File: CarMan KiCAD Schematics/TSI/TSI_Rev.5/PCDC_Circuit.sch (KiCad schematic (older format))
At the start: 56 parts, among them IC4 TS431ILT, K1 APAN3105, Q1 ZVP1320F, Q5 SI1302DL-T1-E3, U10 74LS00PowerPins, U12 REF3033, U19 74HC00, U20 MC7805BDTRKG, U21 MCP6004, U29 SN74LVC1G08DCKR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

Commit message: Added footprints for MCP6004
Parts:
- U21, U35, U40: footprint (none) -> TSI_Rev_2021_Footprint_Lib:SOIC127P600X175-14N
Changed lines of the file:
@@
 F 0 "U21" H 3950 3600 50  0000 C CNN
 F 1 "MCP6004" H 4150 3450 50  0000 C CNN
-F 2 "" H 3950 3700 50  0001 C CNN
+F 2 "TSI_Rev_2021_Footprint_Lib:SOIC127P600X175-14N" H 3950 3700 50  0001 C CNN
 F 3 "http://ww1.microchip.com/downloads/en/DeviceDoc/21733j.pdf" H 4050 3800 50  0001 C CNN
 	4    4000 3600
@@
 F 0 "U21" H 3950 2750 50  0000 C CNN
 F 1 "MCP6004" H 4150 2600 50  0000 C CNN
-F 2 "" H 3950 2850 50  0001 C CNN
+F 2 "TSI_Rev_2021_Footprint_Lib:SOIC127P600X175-14N" H 3950 2850 50  0001 C CNN
 F 3 "http://ww1.microchip.com/downloads/en/DeviceDoc/21733j.pdf" H 4050 2950 50  0001 C CNN
 	3    4000 2750
@@
 F 0 "U40" H 5308 2896 50  0001 L CNN
 F 1 "MCP6004" H 5308 2850 50  0001 L CNN
-F 2 "" H 5300 2950 50  0001 C CNN
+F 2 "TSI_Rev_2021_Footprint_Lib:SOIC127P600X175-14N" H 5300 2950 50  0001 C CNN
 F 3 "http://ww1.microchip.com/downloads/en/DeviceDoc/21733j.pdf" H 5400 3050 50  0001 C CNN
 	5    5350 2850
@@
 F 0 "U40" H 5400 2850 50  0000 C CNN
 F 1 "MCP6004" H 5500 3000 50  0000 C CNN
-F 2 "" H 5300 2950 50  0001 C CNN
+F 2 "TSI_Rev_2021_Footprint_Lib:SOIC127P600X175-14N" H 5300 2950 50  0001 C CNN
 F 3 "http://ww1.microchip.com/downloads/en/DeviceDoc/21733j.pdf" H 5400 3050 50  0001 C CNN
 	1    5350 2850
@@
 F 0 "U40" H 5350 3500 50  0000 C CNN
 F 1 "MCP6004" H 5450 3700 50  0000 C CNN
-F 2 "" H 5300 3600 50  0001 C CNN
+F 2 "TSI_Rev_2021_Footprint_Lib:SOIC127P600X175-14N" H 5300 3600 50  0001 C CNN
 F 3 "http://ww1.microchip.com/downloads/en/DeviceDoc/21733j.pdf" H 5400 3700 50  0001 C CNN
 	2    5350 3500
@@
 F 0 "U40" H 10550 4150 50  0000 C CNN
 F 1 "MCP6004" H 10550 4426 50  0000 C CNN
-F 2 "" H 10500 4250 50  0001 C CNN
+F 2 "TSI_Rev_2021_Footprint_Lib:SOIC127P600X175-14N" H 10500 4250 50  0001 C CNN
 F 3 "http://ww1.microchip.com/downloads/en/DeviceDoc/21733j.pdf" H 10600 4350 50  0001 C CNN
 	4    10550 4150
@@
 F 0 "U35" H 3650 8300 50  0000 C CNN
 F 1 "MCP6004" H 3850 8450 50  0000 C CNN
-F 2 "" H 3600 8400 50  0001 C CNN
+F 2 "TSI_Rev_2021_Footprint_Lib:SOIC127P600X175-14N" H 3600 8400 50  0001 C CNN
 F 3 "http://ww1.microchip.com/downloads/en/DeviceDoc/21733j.pdf" H 3700 8500 50  0001 C CNN
 	1    3650 8300
@@
 F 0 "U35" H 3608 8300 50  0001 L CNN
 F 1 "MCP6004" H 3608 8255 50  0001 L CNN
-F 2 "" H 3600 8400 50  0001 C CNN
+F 2 "TSI_Rev_2021_Footprint_Lib:SOIC127P600X175-14N" H 3600 8400 50  0001 C CNN
 F 3 "http://ww1.microchip.com/downloads/en/DeviceDoc/21733j.pdf" H 3700 8500 50  0001 C CNN
 	5    3650 8300

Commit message: TSI Footprints - Res, Caps, Inductor all 0805s - Mounting Holes
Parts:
- C1, C12, C2, C54, C55: footprint (none) -> Capacitor_SMD:C_0805_2012Metric_Pad1.15x1.40mm_HandSolder
- L1: footprint (none) -> Inductor_SMD:L_0805_2012Metric_Pad1.15x1.40mm_HandSolder
- PS1: footprint TSI_Rev_2021_Footprint_Lib:DIP762W50P254L730H410Q6 -> (none)
- R101, R108, R109, R111, R112, R2, R33, R4, R46, R47, R54, R56, R67, R69, R70, R73, R75: footprint (none) -> Resistor_SMD:R_0805_2012Metric_Pad1.15x1.40mm_HandSolder
- U29: footprint SOT65P210X110-5N -> TSI_Rev_2021_Footprint_Lib:SOT65P210X110-5N
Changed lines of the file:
@@
 F 0 "R2" H 4570 1996 50  0000 L CNN
 F 1 "95K" V 4500 1900 50  0000 L CNN
-F 2 "" V 4430 1950 50  0001 C CNN
+F 2 "Resistor_SMD:R_0805_2012Metric_Pad1.15x1.40mm_HandSolder" V 4430 1950 50  0001 C CNN
 F 3 "~" H 4500 1950 50  0001 C CNN
 	1    4500 1950
@@
 F 0 "C55" V 6450 2350 50  0000 C CNN
 F 1 "0.1u" V 6450 2050 50  0000 C CNN
-F 2 "" H 6550 2200 50  0001 C CNN
+F 2 "Capacitor_SMD:C_0805_2012Metric_Pad1.15x1.40mm_HandSolder" H 6550 2200 50  0001 C CNN
 F 3 "~" H 6550 2200 50  0001 C CNN
 	1    6550 2200
@@
 F 0 "R4" V 9750 3050 50  0000 C CNN
 F 1 "5K" V 9850 3050 50  0000 C CNN
-F 2 "" V 9780 3050 50  0001 C CNN
+F 2 "Resistor_SMD:R_0805_2012Metric_Pad1.15x1.40mm_HandSolder" V 9780 3050 50  0001 C CNN
 F 3 "~" H 9850 3050 50  0001 C CNN
 	1    9850 3050
@@
 F 0 "R56" V 9400 3850 50  0000 C CNN
 F 1 "56K" V 9500 3850 50  0000 C CNN
-F 2 "" V 9430 3850 50  0001 C CNN
+F 2 "Resistor_SMD:R_0805_2012Metric_Pad1.15x1.40mm_HandSolder" V 9430 3850 50  0001 C CNN
 F 3 "~" H 9500 3850 50  0001 C CNN
 	1    9500 3850
@@
 F 0 "C54" H 9600 4250 50  0000 C CNN
 F 1 "15u" H 9600 4450 50  0000 C CNN
-F 2 "" H 9500 4350 50  0001 C CNN
+F 2 "Capacitor_SMD:C_0805_2012Metric_Pad1.15x1.40mm_HandSolder" H 9500 4350 50  0001 C CNN
 F 3 "~" H 9500 4350 50  0001 C CNN
 	1    9500 4350
@@
 F 0 "R67" V 10400 2250 50  0000 C CNN
 F 1 "2.4K" V 10500 2250 50  0000 C CNN
-F 2 "" V 10430 2250 50  0001 C CNN
+F 2 "Resistor_SMD:R_0805_2012Metric_Pad1.15x1.40mm_HandSolder" V 10430 2250 50  0001 C CNN
 F 3 "~" H 10500 2250 50  0001 C CNN
 	1    10500 2250
@@
 F 0 "R69" V 12500 3250 50  0000 C CNN
 F 1 "500" V 12600 3250 50  0000 C CNN
-F 2 "" V 12530 3250 50  0001 C CNN
+F 2 "Resistor_SMD:R_0805_2012Metric_Pad1.15x1.40mm_HandSolder" V 12530 3250 50  0001 C CNN
 F 3 "~" H 12600 3250 50  0001 C CNN
 	1    12600 3250
@@
 F 0 "R111" V 6350 6250 50  0000 L CNN
 F 1 "10K" V 6250 6300 50  0000 L CNN
-F 2 "" V 6180 6350 50  0001 C CNN
+F 2 "Resistor_SMD:R_0805_2012Metric_Pad1.15x1.40mm_HandSolder" V 6180 6350 50  0001 C CNN
 F 3 "~" H 6250 6350 50  0001 C CNN
 	1    6250 6350
@@
 F 0 "R109" V 7300 6000 50  0000 L CNN
 F 1 "1M" V 7200 6050 50  0000 L CNN
-F 2 "" V 7130 6100 50  0001 C CNN
+F 2 "Resistor_SMD:R_0805_2012Metric_Pad1.15x1.40mm_HandSolder" V 7130 6100 50  0001 C CNN
 F 3 "~" H 7200 6100 50  0001 C CNN
 	1    7200 6100
@@
 F 0 "R108" V 5200 6250 50  0000 L CNN
 F 1 "2.4K" V 5100 6250 50  0000 L CNN
-F 2 "" V 5030 6350 50  0001 C CNN
+F 2 "Resistor_SMD:R_0805_2012Metric_Pad1.15x1.40mm_HandSolder" V 5030 6350 50  0001 C CNN
 F 3 "~" H 5100 6350 50  0001 C CNN
 	1    5100 6350
@@
 F 0 "R70" V 5200 7050 50  0000 L CNN
 F 1 "2.4K" V 5100 7050 50  0000 L CNN
-F 2 "" V 5030 7150 50  0001 C CNN
+F 2 "Resistor_SMD:R_0805_2012Metric_Pad1.15x1.40mm_HandSolder" V 5030 7150 50  0001 C CNN
 F 3 "~" H 5100 7150 50  0001 C CNN
 	1    5100 7150
@@
 F 0 "C1" H 11650 9150 50  0000 L CNN
 F 1 "0.47u" H 11650 8950 50  0000 L CNN
-F 2 "" H 11600 9050 50  0001 C CNN
+F 2 "Capacitor_SMD:C_0805_2012Metric_Pad1.15x1.40mm_HandSolder" H 11600 9050 50  0001 C CNN
 F 3 "~" H 11600 9050 50  0001 C CNN
 	1    11600 9050
@@
 F 0 "R33" V 5200 10300 50  0000 L CNN
 F 1 "5K" V 5100 10350 50  0000 L CNN
-F 2 "" V 5030 10400 50  0001 C CNN
+F 2 "Resistor_SMD:R_0805_2012Metric_Pad1.15x1.40mm_HandSolder" V 5030 10400 50  0001 C CNN
 F 3 "~" H 5100 10400 50  0001 C CNN
 	1    5100 10400
@@
 F 0 "R54" V 6450 10500 50  0000 L CNN
 F 1 "2.4K" V 6350 10500 50  0000 L CNN
-F 2 "" V 6280 10600 50  0001 C CNN
+F 2 "Resistor_SMD:R_0805_2012Metric_Pad1.15x1.40mm_HandSolder" V 6280 10600 50  0001 C CNN
 F 3 "~" H 6350 10600 50  0001 C CNN
 	1    6350 10600
@@
 F 0 "PS1" H 5725 10081 79  0000 C CNN
 F 1 "THN_30-2415WI" H 5725 9946 79  0000 C CNN
-F 2 "TSI_Rev_2021_Footprint_Lib:DIP762W50P254L730H410Q6" H 5500 9700 79  0001 C CNN
+F 2 "" H 5500 9700 79  0001 C CNN
 F 3 "https://www.snapeda.com/parts/THN%2030-2415WI/Traco%20Power/datasheet/" H 5500 9700 79  0001 C CNN
 	1    5750 9650
@@
 F 0 "R73" V 6350 8600 50  0000 L CNN
 F 1 "5K" V 6250 8650 50  0000 L CNN
-F 2 "" V 6180 8700 50  0001 C CNN
+F 2 "Resistor_SMD:R_0805_2012Metric_Pad1.15x1.40mm_HandSolder" V 6180 8700 50  0001 C CNN
 F 3 "~" H 6250 8700 50  0001 C CNN
 	1    6250 8700
@@
 F 0 "R75" V 6350 7450 50  0000 L CNN
 F 1 "5K" V 6250 7500 50  0000 L CNN
-F 2 "" V 6180 7550 50  0001 C CNN
+F 2 "Resistor_SMD:R_0805_2012Metric_Pad1.15x1.40mm_HandSolder" V 6180 7550 50  0001 C CNN
 F 3 "~" H 6250 7550 50  0001 C CNN
 	1    6250 7550
@@
 F 0 "R112" V 3400 7550 50  0000 L CNN
 F 1 "330" V 3300 7600 50  0000 L CNN
-F 2 "" V 3230 7650 50  0001 C CNN
+F 2 "Resistor_SMD:R_0805_2012Metric_Pad1.15x1.40mm_HandSolder" V 3230 7650 50  0001 C CNN
 F 3 "~" H 3300 7650 50  0001 C CNN
 	1    3300 7650
@@
 F 0 "C12" H 14600 8950 50  0000 C CNN
 F 1 "0.33u" H 14600 9150 50  0000 C CNN
-F 2 "" H 14500 9050 50  0001 C CNN
+F 2 "Capacitor_SMD:C_0805_2012Metric_Pad1.15x1.40mm_HandSolder" H 14500 9050 50  0001 C CNN
 F 3 "~" H 14500 9050 50  0001 C CNN
 	1    14500 9050
@@
 F 0 "R46" V 12800 7650 50  0000 L CNN
 F 1 "1K" V 12700 7700 50  0000 L CNN
-F 2 "" V 12630 7750 50  0001 C CNN
+F 2 "Resistor_SMD:R_0805_2012Metric_Pad1.15x1.40mm_HandSolder" V 12630 7750 50  0001 C CNN
 F 3 "~" H 12700 7750 50  0001 C CNN
 	1    12700 7750
@@
 F 0 "R101" V 14450 7850 50  0000 L CNN
 F 1 "10K" V 14350 7900 50  0000 L CNN
-F 2 "" V 14280 7950 50  0001 C CNN
+F 2 "Resistor_SMD:R_0805_2012Metric_Pad1.15x1.40mm_HandSolder" V 14280 7950 50  0001 C CNN
 F 3 "~" H 14350 7950 50  0001 C CNN
 	1    14350 7950
@@
 F 0 "R47" V 5200 8200 50  0000 L CNN
 F 1 "500" V 5100 8200 50  0000 L CNN
-F 2 "" V 5030 8300 50  0001 C CNN
+F 2 "Resistor_SMD:R_0805_2012Metric_Pad1.15x1.40mm_HandSolder" V 5030 8300 50  0001 C CNN
 F 3 "~" H 5100 8300 50  0001 C CNN
 	1    5100 8300
@@
 F 0 "U29" H 6350 4100 50  0000 C CNN
 F 1 "SN74LVC1G08DCKR" H 6600 4000 50  0000 C CNN
-F 2 "SOT65P210X110-5N" H 6500 4250 50  0001 L BNN
+F 2 "TSI_Rev_2021_Footprint_Lib:SOT65P210X110-5N" H 6500 4250 50  0001 L BNN
 F 3 "https://www.ti.com/store/ti/en/p/product/?p=SN74LVC1G08DCKR&HQS=OCB-tistore-invf-partpage-invf-store-SnapEDA-wwe" H 6500 4250 50  0001 L BNN
 F 4 "Unavailable" H 6500 4250 50  0001 L BNN "AVAILABILITY"
@@
 F 0 "U29" H 6628 4296 50  0001 L CNN
 F 1 "SN74LVC1G08DCKR" H 6628 4250 50  0001 L CNN
-F 2 "SOT65P210X110-5N" H 6500 4250 50  0001 L BNN
+F 2 "TSI_Rev_2021_Footprint_Lib:SOT65P210X110-5N" H 6500 4250 50  0001 L BNN
 F 3 "https://www.ti.com/store/ti/en/p/product/?p=SN74LVC1G08DCKR&HQS=OCB-tistore-invf-partpage-invf-store-SnapEDA-wwe" H 6500 4250 50  0001 L BNN
 F 4 "Unavailable" H 6500 4250 50  0001 L BNN "AVAILABILITY"
@@
 F 0 "C2" H 4250 9250 50  0000 C CNN
 F 1 "4.7u" H 4250 9450 50  0000 C CNN
-F 2 "" H 4150 9350 50  0001 C CNN
+F 2 "Capacitor_SMD:C_0805_2012Metric_Pad1.15x1.40mm_HandSolder" H 4150 9350 50  0001 C CNN
 F 3 "~" H 4150 9350 50  0001 C CNN
 	1    4150 9350
@@
 F 0 "L1" H 4500 9315 50  0000 C CNN
 F 1 "2.2uH" H 4500 9224 50  0000 C CNN
-F 2 "" H 4500 9100 50  0001 C CNN
+F 2 "Inductor_SMD:L_0805_2012Metric_Pad1.15x1.40mm_HandSolder" H 4500 9100 50  0001 C CNN
 F 3 "~" H 4500 9100 50  0001 C CNN
 	1    4500 9100

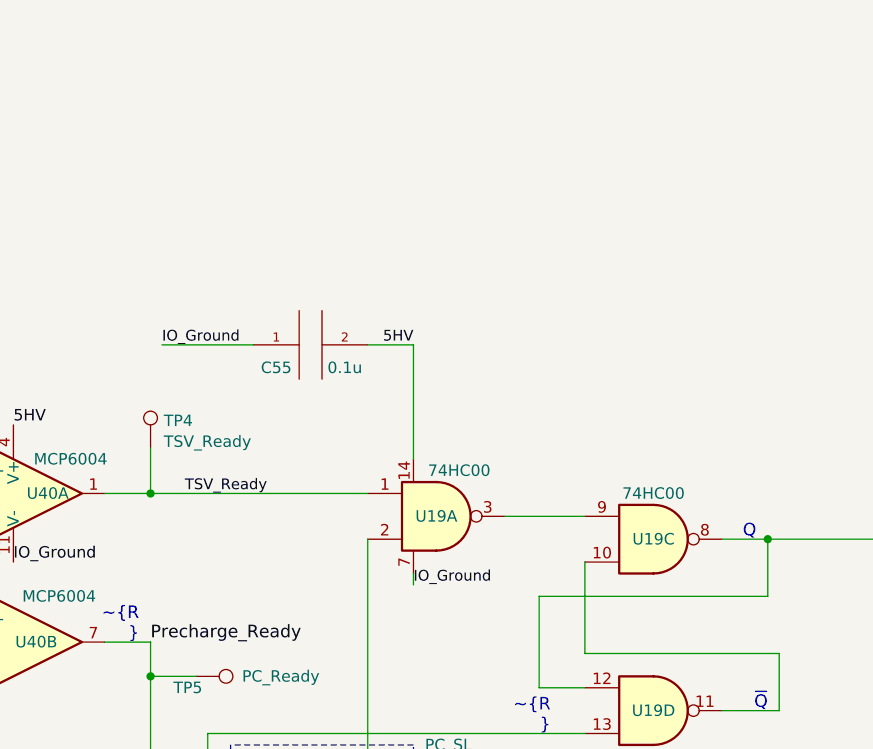
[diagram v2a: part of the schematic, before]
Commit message: TSI Footprinting (~80%)  - Added Molex  - Added Current Sensor
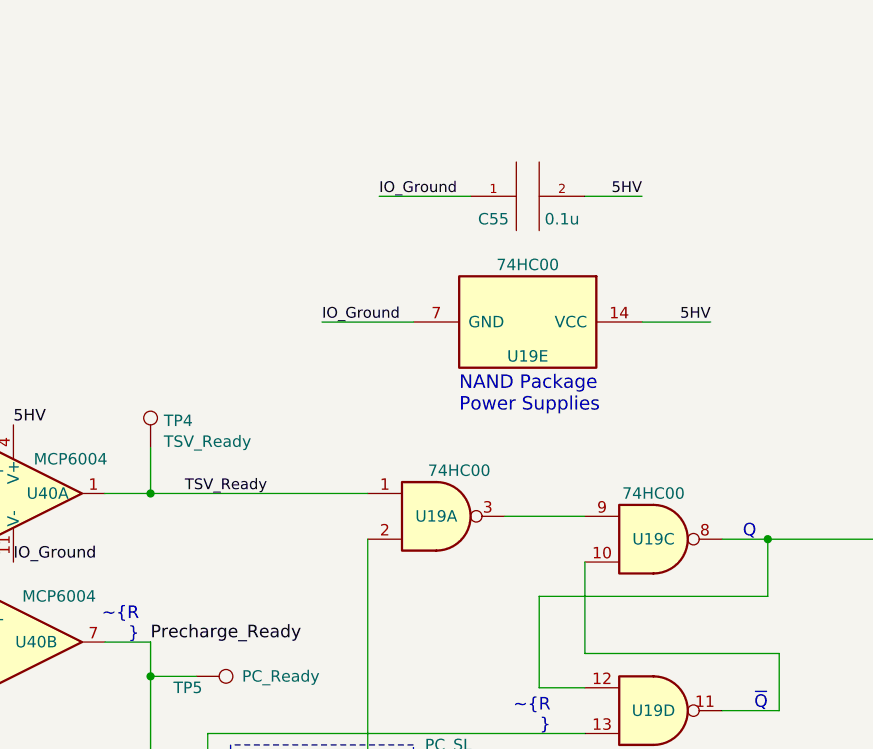
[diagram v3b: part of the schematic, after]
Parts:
- removed U10: 74LS00PowerPins, symbol TSI_Rev.5-rescue:74LS00PowerPins-CarMan_KiCAD_Library-TSI_Rev.5-rescue
- added unit 5 of U19
- TP4, TP5, TP6, TP7: footprint (none) -> TestPoint:TestPoint_Pad_D3.0mm
- U19: footprint (none) -> TSI_Rev_2021_Footprint_Lib:SOIC127P600X175-14N
- U20: footprint (none) -> TSI_Rev_2021_Footprint_Lib:DPAK229P990X238-4N
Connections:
- net 5HV: now also U19.14 (VCC)
- net DC_RELAY-: now also U19.7 (GND)
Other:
- note added: "NAND Package \nPower Supplies"
- moved on the sheet: C55
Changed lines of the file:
@@
 F 0 "U19" H 7100 2950 50  0000 C CNN
 F 1 "74HC00" H 7200 3150 50  0000 C CNN
-F 2 "" H 7100 2950 50  0001 C CNN
+F 2 "TSI_Rev_2021_Footprint_Lib:SOIC127P600X175-14N" H 7100 2950 50  0001 C CNN
 F 3 "http://www.ti.com/lit/gpn/sn74hc00" H 7100 2950 50  0001 C CNN
 	1    7100 2950
 	1    0    0    -1
 $EndComp
-$Comp
-L TSI_Rev.5-rescue:74LS00PowerPins-CarMan_KiCAD_Library-TSI_Rev.5-rescue U10
-U 1 1 619B0A27
-P 7100 2950
-F 0 "U10" H 7044 2950 50  0001 L CNN
-F 1 "74LS00PowerPins" H 7044 2905 50  0001 L CNN
-F 2 "" H 7100 2950 50  0001 C CNN
-F 3 "http://www.ti.com/lit/gpn/sn74ls00" H 7100 2950 50  0001 C CNN
-	1    7100 2950
-	1    0    0    -1
-$EndComp
-Text Label 7000 2200 2    47   ~ 0
+Text Label 8300 2100 2    47   ~ 0
 5HV
 $Comp
@@
 F 0 "U19" H 5400 4300 50  0000 C CNN
 F 1 "74HC00" H 5400 4534 50  0000 C CNN
-F 2 "" H 5400 4300 50  0001 C CNN
+F 2 "TSI_Rev_2021_Footprint_Lib:SOIC127P600X175-14N" H 5400 4300 50  0001 C CNN
 F 3 "http://www.ti.com/lit/gpn/sn74hc00" H 5400 4300 50  0001 C CNN
 	2    5400 4300
@@
 F 0 "U19" H 8050 3050 50  0000 C CNN
 F 1 "74HC00" H 8050 3250 50  0000 C CNN
-F 2 "" H 8050 3050 50  0001 C CNN
+F 2 "TSI_Rev_2021_Footprint_Lib:SOIC127P600X175-14N" H 8050 3050 50  0001 C CNN
 F 3 "http://www.ti.com/lit/gpn/sn74hc00" H 8050 3050 50  0001 C CNN
 	3    8050 3050
 	1    0    0    -1
 $EndComp
-Wire Wire Line
-	7000 3200 7000 3250
 $Comp
 L pspice:CAP C?
 U 1 1 619C449A
-P 6550 2200
+P 7500 1550
 AR Path="/5FC85F57/619C449A" Ref="C?"  Part="1"
 AR Path="/6196BF15/619C449A" Ref="C55"  Part="1"
-F 0 "C55" V 6450 2350 50  0000 C CNN
-F 1 "0.1u" V 6450 2050 50  0000 C CNN
-F 2 "Capacitor_SMD:C_0805_2012Metric_Pad1.15x1.40mm_HandSolder" H 6550 2200 50  0001 C CNN
-F 3 "~" H 6550 2200 50  0001 C CNN
-	1    6550 2200
+F 0 "C55" V 7400 1700 50  0000 C CNN
+F 1 "0.1u" V 7400 1400 50  0000 C CNN
+F 2 "Capacitor_SMD:C_0805_2012Metric_Pad1.15x1.40mm_HandSolder" H 7500 1550 50  0001 C CNN
+F 3 "~" H 7500 1550 50  0001 C CNN
+	1    7500 1550
 	0    -1   -1   0
 $EndComp
@@
 F 0 "TP4" H 5908 2768 50  0000 L CNN
 F 1 "TSV_Ready" H 5908 2677 50  0000 L CNN
-F 2 "" H 6050 2650 50  0001 C CNN
+F 2 "TestPoint:TestPoint_Pad_D3.0mm" H 6050 2650 50  0001 C CNN
 F 3 "~" H 6050 2650 50  0001 C CNN
 	1    5850 2650
@@
 F 0 "U19" H 8050 3800 50  0000 C CNN
 F 1 "74HC00" H 8050 3600 50  0000 C CNN
-F 2 "" H 8050 3800 50  0001 C CNN
+F 2 "TSI_Rev_2021_Footprint_Lib:SOIC127P600X175-14N" H 8050 3800 50  0001 C CNN
 F 3 "http://www.ti.com/lit/gpn/sn74hc00" H 8050 3800 50  0001 C CNN
 	4    8050 3800
@@
 F 0 "TP5" V 6100 3550 50  0000 L CNN
 F 1 "PC_Ready" V 6050 3850 50  0000 L CNN
-F 2 "" H 6250 3650 50  0001 C CNN
+F 2 "TestPoint:TestPoint_Pad_D3.0mm" H 6250 3650 50  0001 C CNN
 F 3 "~" H 6250 3650 50  0001 C CNN
 	1    6050 3650
@@
 F 0 "TP6" H 7150 4200 50  0000 L CNN
 F 1 "PC_SL" H 7050 4350 50  0000 L CNN
-F 2 "" H 7350 4150 50  0001 C CNN
+F 2 "TestPoint:TestPoint_Pad_D3.0mm" H 7350 4150 50  0001 C CNN
 F 3 "~" H 7350 4150 50  0001 C CNN
 	1    7150 4150
@@
 F 0 "TP7" H 2700 8100 50  0000 L CNN
 F 1 "SL_TP" H 2600 8250 50  0000 L CNN
-F 2 "" H 2900 8050 50  0001 C CNN
+F 2 "TestPoint:TestPoint_Pad_D3.0mm" H 2900 8050 50  0001 C CNN
 F 3 "~" H 2900 8050 50  0001 C CNN
 	1    2700 8050
@@
 F 0 "U20" H 15000 9308 79  0000 C CNN
 F 1 "MC7805BDTRKG" H 15000 9173 79  0000 C CNN
-F 2 "" H 15000 9150 79  0001 C CNN
-F 3 "" H 15000 9150 79  0001 C CNN
+F 2 "TSI_Rev_2021_Footprint_Lib:DPAK229P990X238-4N" H 15000 9150 79  0001 C CNN
+F 3 "https://www.snapeda.com/parts/MC7805BDTRKG/ON%20Semiconductor/view-part/?ref=search&t=mc7805bdtrkg" H 15000 9150 79  0001 C CNN
 	1    15000 8900
 	1    0    0    -1
@@
 	1    0    0    -1
 $EndComp
-Text Label 7000 3250 0    47   ~ 0
-IO_Ground
-Text Label 5900 2200 0    47   ~ 0
-IO_Ground
-Wire Wire Line
-	5900 2200 6300 2200
-Wire Wire Line
-	6800 2200 7000 2200
-Wire Wire Line
-	7000 2700 7000 2200
+Text Label 6600 2100 0    47   ~ 0
+IO_Ground
+Text Label 6850 1550 0    47   ~ 0
+IO_Ground
+Wire Wire Line
+	6850 1550 7250 1550
 Wire Wire Line
 	9000 4800 9500 4800
@@
 Wire Wire Line
 	4900 9100 4900 9500
+$Comp
+L 74xx:74HC00 U19
+U 5 1 60014D73
+P 7500 2100
+F 0 "U19" V 7650 2100 50  0000 C CNN
+F 1 "74HC00" V 7250 2100 50  0000 C CNN
+F 2 "TSI_Rev_2021_Footprint_Lib:SOIC127P600X175-14N" H 7500 2100 50  0001 C CNN
+F 3 "http://www.ti.com/lit/gpn/sn74hc00" H 7500 2100 50  0001 C CNN
+	5    7500 2100
+	0    1    1    0
+$EndComp
+Wire Wire Line
+	8000 2100 8300 2100
+Wire Wire Line
+	7000 2100 6600 2100
+Text Label 8000 1550 2    47   ~ 0
+5HV
+Wire Wire Line
+	8000 1550 7750 1550
+Text Notes 7200 2500 0    59   ~ 0
+NAND Package \nPower Supplies
 $EndSCHEMATC

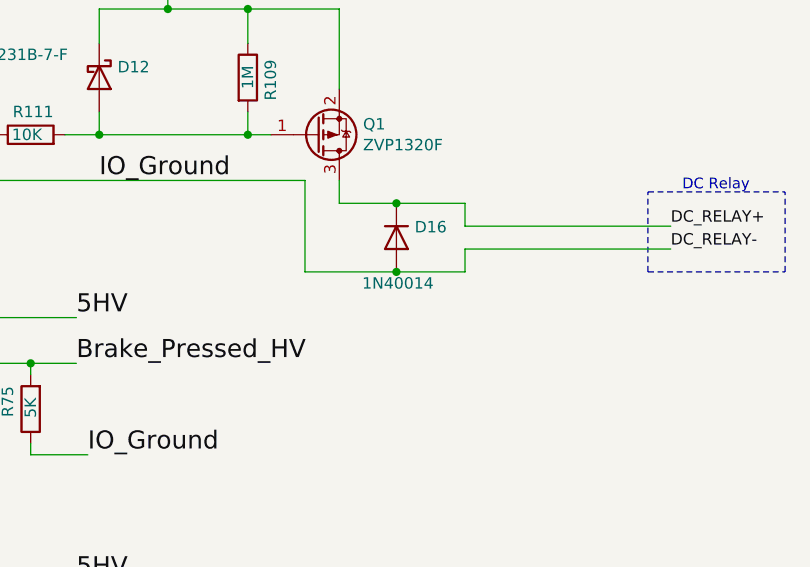
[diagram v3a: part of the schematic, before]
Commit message: TSI Footprinting (~90%)
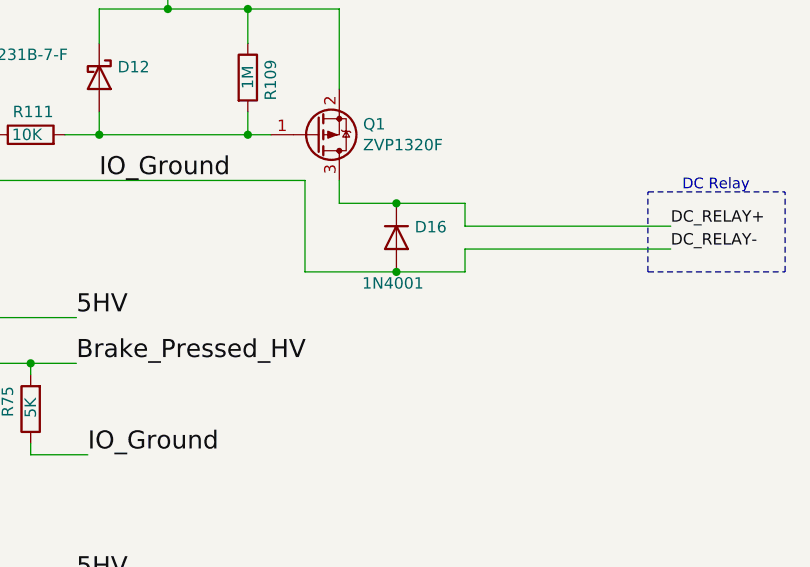
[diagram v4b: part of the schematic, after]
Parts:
- D14, D6, D7: footprint (none) -> LED_SMD:LED_0805_2012Metric_Pad1.15x1.40mm_HandSolder
- D16: value 1N40014 -> 1N4001; footprint (none) -> Diode_THT:D_DO-41_SOD81_P7.62mm_Horizontal
- D17, D8: footprint (none) -> Diode_THT:D_DO-41_SOD81_P7.62mm_Horizontal
- JP4, JP5: footprint (none) -> Connector_PinHeader_2.54mm:PinHeader_1x02_P2.54mm_Vertical
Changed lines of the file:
@@
 F 0 "D17" V 10904 2530 50  0000 L CNN
 F 1 "1N4001" H 10800 2350 50  0000 L CNN
-F 2 "" H 10950 2450 50  0001 C CNN
+F 2 "Diode_THT:D_DO-41_SOD81_P7.62mm_Horizontal" H 10950 2450 50  0001 C CNN
 F 3 "~" H 10950 2450 50  0001 C CNN
 	1    10950 2450
@@
 F 0 "JP5" V 10996 3262 50  0000 R CNN
 F 1 "Jumper" V 10905 3262 50  0000 R CNN
-F 2 "" H 10950 3350 50  0001 C CNN
+F 2 "Connector_PinHeader_2.54mm:PinHeader_1x02_P2.54mm_Vertical" H 10950 3350 50  0001 C CNN
 F 3 "~" H 10950 3350 50  0001 C CNN
 	1    10950 3350
@@
 F 0 "D6" V 10550 2600 50  0000 R CNN
 F 1 "LED" H 10550 2750 50  0000 R CNN
-F 2 "" H 10500 2650 50  0001 C CNN
+F 2 "LED_SMD:LED_0805_2012Metric_Pad1.15x1.40mm_HandSolder" H 10500 2650 50  0001 C CNN
 F 3 "~" H 10500 2650 50  0001 C CNN
 	1    10500 2650
@@
 F 0 "JP4" V 12446 4112 50  0000 R CNN
 F 1 "Jumper" V 12355 4112 50  0000 R CNN
-F 2 "" H 12400 4200 50  0001 C CNN
+F 2 "Connector_PinHeader_2.54mm:PinHeader_1x02_P2.54mm_Vertical" H 12400 4200 50  0001 C CNN
 F 3 "~" H 12400 4200 50  0001 C CNN
 	1    12400 4200
@@
 F 0 "D8" V 13004 3530 50  0000 L CNN
 F 1 "1N4001" H 12900 3350 50  0000 L CNN
-F 2 "" H 13050 3450 50  0001 C CNN
+F 2 "Diode_THT:D_DO-41_SOD81_P7.62mm_Horizontal" H 13050 3450 50  0001 C CNN
 F 3 "~" H 13050 3450 50  0001 C CNN
 	1    13050 3450
@@
 F 0 "D7" V 12650 3600 50  0000 R CNN
 F 1 "LED" H 12650 3750 50  0000 R CNN
-F 2 "" H 12600 3650 50  0001 C CNN
+F 2 "LED_SMD:LED_0805_2012Metric_Pad1.15x1.40mm_HandSolder" H 12600 3650 50  0001 C CNN
 F 3 "~" H 12600 3650 50  0001 C CNN
 	1    12600 3650
@@
 F 0 "D14" H 3700 7550 50  0000 C CNN
 F 1 "SL_Status" H 3700 7750 50  0000 C CNN
-F 2 "" H 3700 7650 50  0001 C CNN
+F 2 "LED_SMD:LED_0805_2012Metric_Pad1.15x1.40mm_HandSolder" H 3700 7650 50  0001 C CNN
 F 3 "~" H 3700 7650 50  0001 C CNN
 	1    3700 7650
@@
 P 7850 6800
 F 0 "D16" V 7804 6880 50  0000 L CNN
-F 1 "1N40014" V 8050 6650 50  0000 L CNN
-F 2 "" H 7850 6800 50  0001 C CNN
+F 1 "1N4001" V 8050 6650 50  0000 L CNN
+F 2 "Diode_THT:D_DO-41_SOD81_P7.62mm_Horizontal" H 7850 6800 50  0001 C CNN
 F 3 "~" H 7850 6800 50  0001 C CNN
 	1    7850 6800
